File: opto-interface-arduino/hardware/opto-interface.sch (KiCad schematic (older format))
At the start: 24 parts, among them P1 CONN_02X06, P2 CONN_01X06, U1 LM7805, U2 LM7905

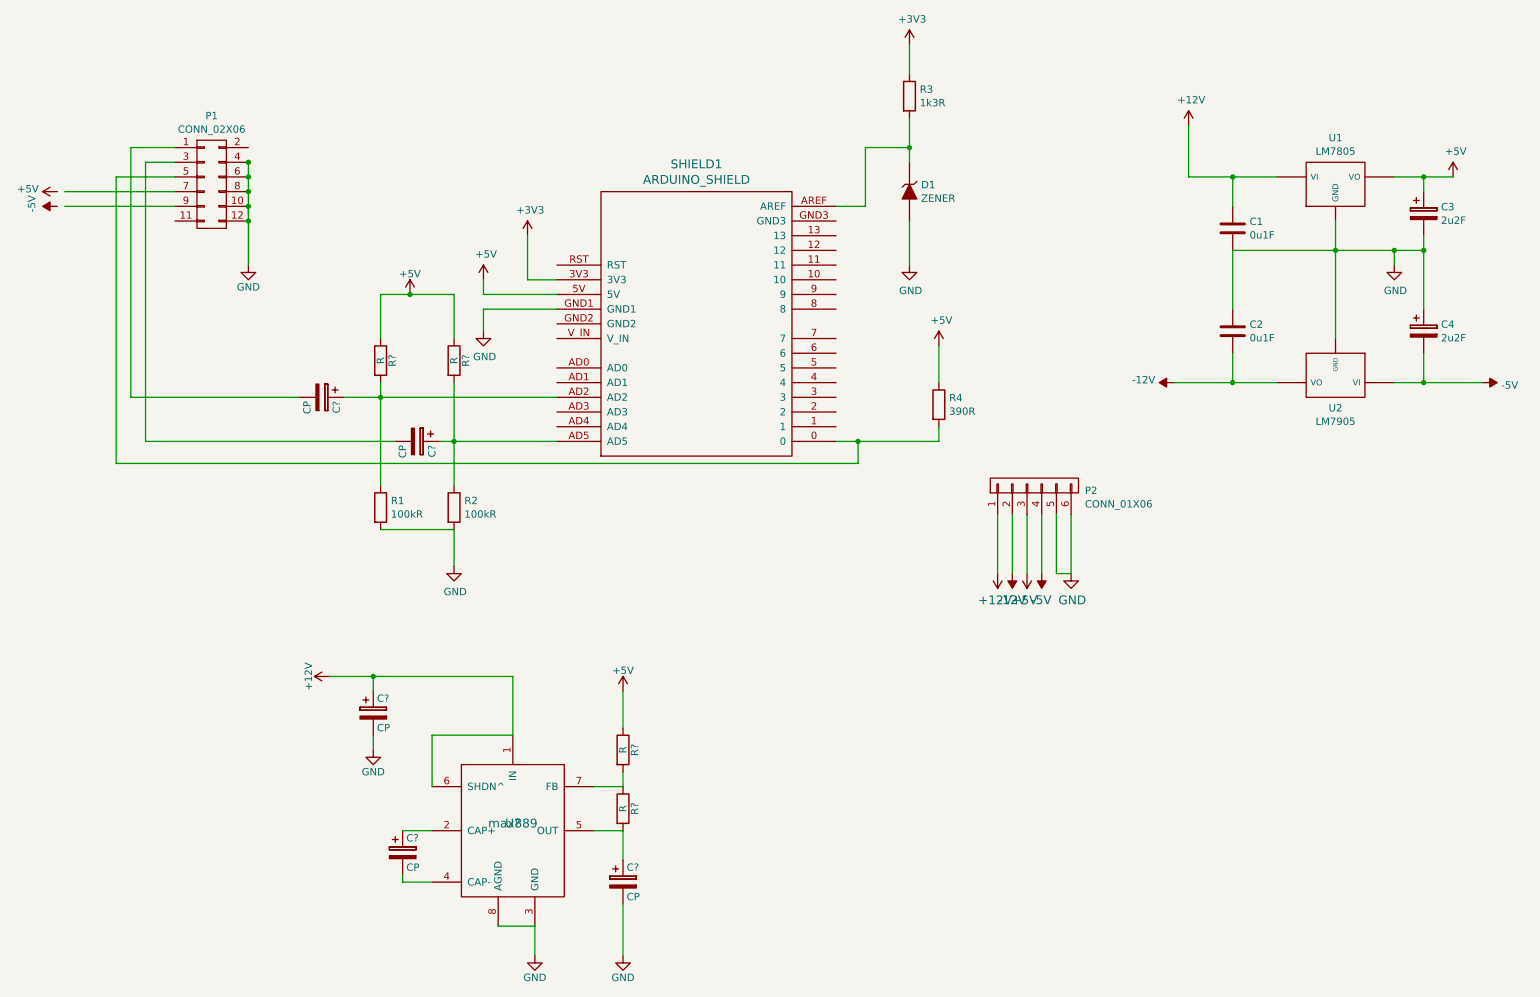
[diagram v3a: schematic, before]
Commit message: Add filter simulations, first pass layout, some calculations and some skeleton code.
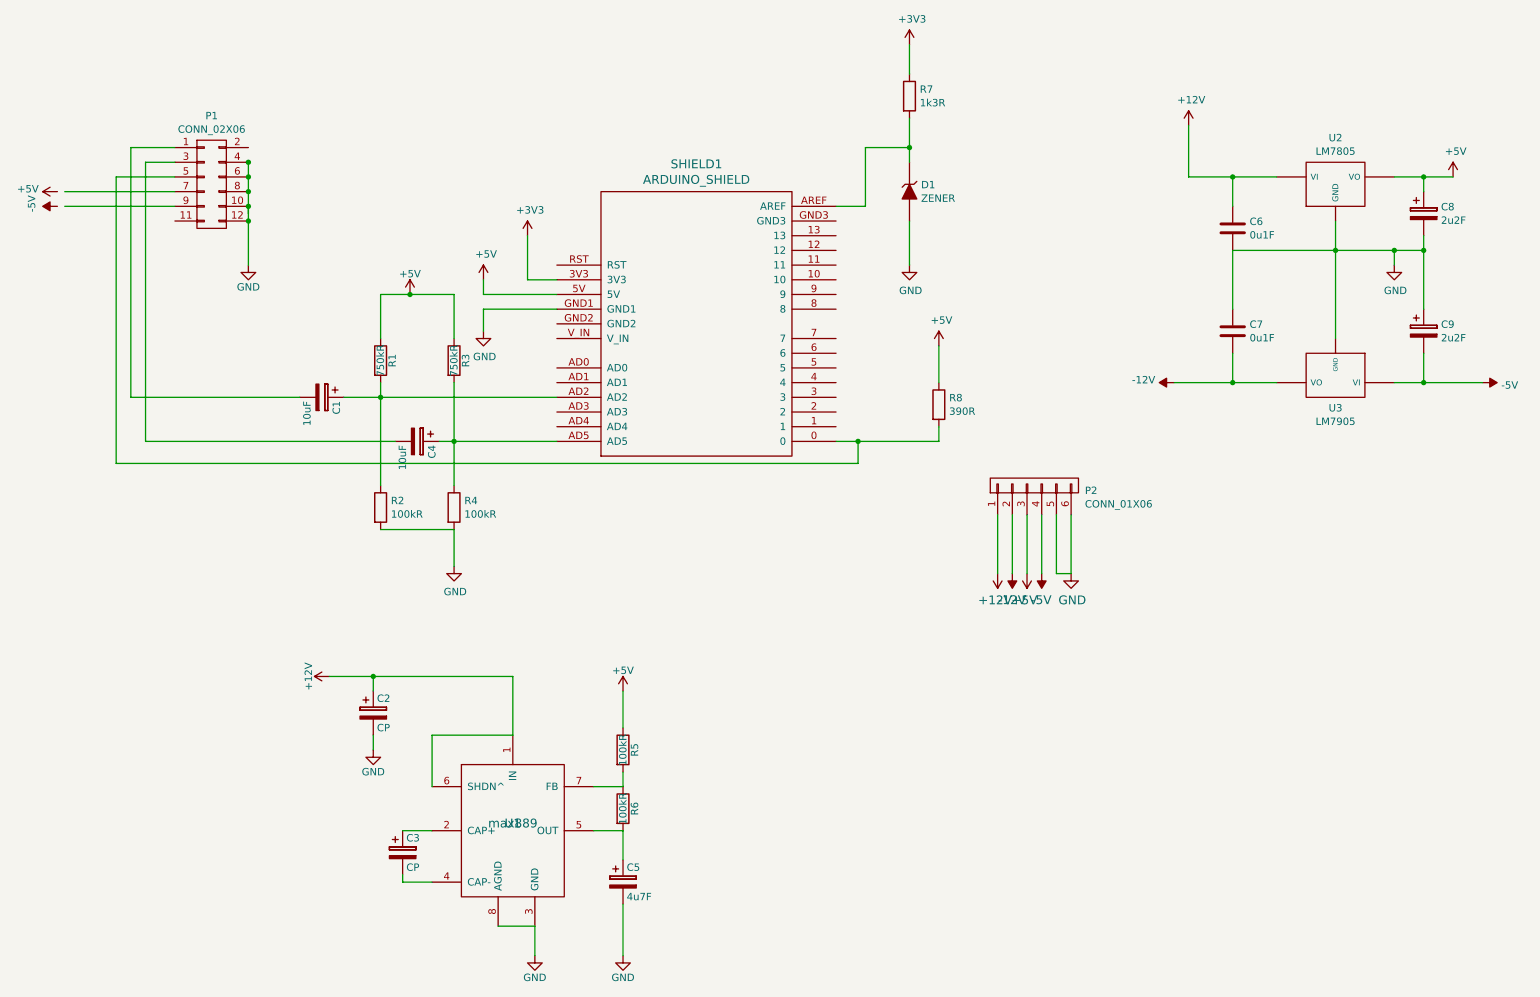
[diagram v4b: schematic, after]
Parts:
- C1, C4: renamed from C?; value CP -> 10uF; footprint (none) -> Discret:CP4
- C2, C3: renamed from C?; footprint (none) -> Capacitors_SMD:c_elec_8x5.4
- C5: renamed from C?; value CP -> 4u7F; footprint (none) -> Capacitors_SMD:c_elec_8x5.4
- R1, R3: renamed from R?; value R -> 750kR; footprint (none) -> Resistors_SMD:R_0805_HandSoldering
- R5, R6: renamed from R?; value R -> 100kR; footprint (none) -> Resistors_SMD:R_0805_HandSoldering
- U1: renamed from U?; footprint (none) -> SMD_Packages:SOIC-8-N
- U2: renamed from U1; footprint TO_SOT_Packages_THT:TO-220_Neutral123_Horizontal_LargePads -> regul:TO-220_regul_Horizontal_LargePads
- U3: renamed from U2; footprint TO_SOT_Packages_THT:TO-220_Neutral123_Horizontal_LargePads -> regul:TO-220_regul_Horizontal_LargePads
- renumbered C1 to C6, C2 to C7, C3 to C8, C4 to C9, R1 to R2, R2 to R4, R3 to R7, R4 to R8
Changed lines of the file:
@@
 $EndComp
 $Comp
-L R-RESCUE-opto-interface R4
+L R-RESCUE-opto-interface R8
 U 1 1 56A61D1F
 P 6600 3150
-F 0 "R4" H 6670 3196 50  0000 L CNN
+F 0 "R8" H 6670 3196 50  0000 L CNN
 F 1 "390R" H 6670 3104 50  0000 L CNN
 F 2 "Resistors_SMD:R_0805_HandSoldering" V 6530 3150 50  0001 C CNN
@@
 $EndComp
 $Comp
-L R-RESCUE-opto-interface R2
+L R-RESCUE-opto-interface R4
 U 1 1 56A61E09
 P 3300 3850
-F 0 "R2" H 3370 3896 50  0000 L CNN
+F 0 "R4" H 3370 3896 50  0000 L CNN
 F 1 "100kR" H 3370 3804 50  0000 L CNN
 F 2 "Resistors_SMD:R_0805_HandSoldering" V 3230 3850 50  0001 C CNN
@@
 $EndComp
 $Comp
-L R-RESCUE-opto-interface R1
+L R-RESCUE-opto-interface R2
 U 1 1 56A61E93
 P 2800 3850
-F 0 "R1" H 2870 3896 50  0000 L CNN
+F 0 "R2" H 2870 3896 50  0000 L CNN
 F 1 "100kR" H 2870 3804 50  0000 L CNN
 F 2 "Resistors_SMD:R_0805_HandSoldering" V 2730 3850 50  0001 C CNN
@@
 $EndComp
 $Comp
-L LM7805 U1
+L LM7805 U2
 U 1 1 56A63641
 P 9300 1650
-F 0 "U1" H 9300 1966 50  0000 C CNN
+F 0 "U2" H 9300 1966 50  0000 C CNN
 F 1 "LM7805" H 9300 1874 50  0000 C CNN
-F 2 "TO_SOT_Packages_THT:TO-220_Neutral123_Horizontal_LargePads" H 9300 1650 50  0001 C CNN
+F 2 "regul:TO-220_regul_Horizontal_LargePads" H 9300 1650 50  0001 C CNN
 F 3 "" H 9300 1650 50  0000 C CNN
 	1    9300 1650
@@
 	9700 1600 10100 1600
 $Comp
-L C-RESCUE-opto-interface C1
+L C-RESCUE-opto-interface C6
 U 1 1 56A63A9E
 P 8600 1950
-F 0 "C1" H 8715 1996 50  0000 L CNN
+F 0 "C6" H 8715 1996 50  0000 L CNN
 F 1 "0u1F" H 8715 1904 50  0000 L CNN
 F 2 "Capacitors_ThroughHole:C_Disc_D6_P5" H 8638 1800 50  0001 C CNN
@@
 Connection ~ 9300 2100
 $Comp
-L CP-RESCUE-opto-interface C3
+L CP-RESCUE-opto-interface C8
 U 1 1 56A63B52
 P 9900 1850
-F 0 "C3" H 10018 1896 50  0000 L CNN
+F 0 "C8" H 10018 1896 50  0000 L CNN
 F 1 "2u2F" H 10018 1804 50  0000 L CNN
 F 2 "Discret:CP5" H 9938 1700 50  0001 C CNN
@@
 Connection ~ 9700 2100
 $Comp
-L LM7905 U2
+L LM7905 U3
 U 1 1 56A63CED
 P 9300 2950
-F 0 "U2" H 9300 3173 50  0000 C CNN
+F 0 "U3" H 9300 3173 50  0000 C CNN
 F 1 "LM7905" H 9300 3265 50  0000 C CNN
-F 2 "TO_SOT_Packages_THT:TO-220_Neutral123_Horizontal_LargePads" H 9300 2950 50  0001 C CNN
+F 2 "regul:TO-220_regul_Horizontal_LargePads" H 9300 2950 50  0001 C CNN
 F 3 "" H 9300 2950 50  0000 C CNN
 	1    9300 2950
@@
 $EndComp
 $Comp
-L C-RESCUE-opto-interface C2
+L C-RESCUE-opto-interface C7
 U 1 1 56A63DBB
 P 8600 2650
-F 0 "C2" H 8715 2696 50  0000 L CNN
+F 0 "C7" H 8715 2696 50  0000 L CNN
 F 1 "0u1F" H 8715 2604 50  0000 L CNN
 F 2 "Capacitors_ThroughHole:C_Disc_D6_P5" H 8638 2500 50  0001 C CNN
@@
 $EndComp
 $Comp
-L CP-RESCUE-opto-interface C4
+L CP-RESCUE-opto-interface C9
 U 1 1 56A63E65
 P 9900 2650
-F 0 "C4" H 10018 2696 50  0000 L CNN
+F 0 "C9" H 10018 2696 50  0000 L CNN
 F 1 "2u2F" H 10018 2604 50  0000 L CNN
 F 2 "Discret:CP5" H 9938 2500 50  0001 C CNN
@@
 $EndComp
 $Comp
-L -12V #PWR15
+L -12V #PWR22
 U 1 1 56A63F07
 P 8200 3000
-F 0 "#PWR15" H 8200 3100 50  0001 C CNN
+F 0 "#PWR22" H 8200 3100 50  0001 C CNN
 F 1 "-12V" V 8218 3127 50  0000 L CNN
 F 2 "" H 8200 3000 50  0000 C CNN
@@
 Connection ~ 9900 2100
 $Comp
-L -5V #PWR19
+L -5V #PWR26
 U 1 1 56A640D9
 P 10300 3000
-F 0 "#PWR19" H 10300 3100 50  0001 C CNN
+F 0 "#PWR26" H 10300 3100 50  0001 C CNN
 F 1 "-5V" V 10318 3128 50  0000 L CNN
 F 2 "" H 10300 3000 50  0000 C CNN
@@
 Connection ~ 6400 1400
 $Comp
-L R-RESCUE-opto-interface R3
+L R-RESCUE-opto-interface R7
 U 1 1 56A8A23F
 P 6400 1050
-F 0 "R3" H 6470 1096 50  0000 L CNN
+F 0 "R7" H 6470 1096 50  0000 L CNN
 F 1 "1k3R" H 6470 1004 50  0000 L CNN
 F 2 "Resistors_SMD:R_0805_HandSoldering" V 6330 1050 50  0001 C CNN
@@
 $EndComp
 $Comp
-L -12V #PWR11
+L -12V #PWR18
 U 1 1 56B5E808
 P 7100 4300
-F 0 "#PWR11" H 7100 4400 20  0001 C CNN
+F 0 "#PWR18" H 7100 4400 20  0001 C CNN
 F 1 "-12V" H 7102 4480 60  0000 C CNN
 F 2 "" H 7100 4300 60  0000 C CNN
@@
 $EndComp
 $Comp
-L -5V #PWR13
+L -5V #PWR20
 U 1 1 56B5E862
 P 7300 4300
-F 0 "#PWR13" H 7300 4400 20  0001 C CNN
+F 0 "#PWR20" H 7300 4400 20  0001 C CNN
 F 1 "-5V" H 7302 4480 60  0000 C CNN
 F 2 "" H 7300 4300 60  0000 C CNN
@@
 	7500 4300 7500 3900
 $Comp
-L max889 U?
+L max889 U1
 U 1 1 56D83630
 P 3700 6000
-F 0 "U?" H 3700 6000 60  0000 C CNN
+F 0 "U1" H 3700 6000 60  0000 C CNN
 F 1 "max889" H 3700 6000 60  0000 C CNN
-F 2 "" H 3700 6000 60  0000 C CNN
+F 2 "SMD_Packages:SOIC-8-N" H 3700 6000 60  0001 C CNN
 F 3 "" H 3700 6000 60  0000 C CNN
 	1    3700 6000
@@
 $EndComp
 $Comp
-L +12V #PWR?
+L +12V #PWR015
 U 1 1 56D96E3B
 P 2450 5000
-F 0 "#PWR?" H 2450 4850 50  0001 C CNN
+F 0 "#PWR015" H 2450 4850 50  0001 C CNN
 F 1 "+12V" H 2450 5140 50  0000 C CNN
 F 2 "" H 2450 5000 50  0000 C CNN
@@
 $EndComp
 $Comp
-L CP C?
+L CP C2
 U 1 1 56D96E9A
 P 2750 5250
-F 0 "C?" H 2775 5350 50  0000 L CNN
+F 0 "C2" H 2775 5350 50  0000 L CNN
 F 1 "CP" H 2775 5150 50  0000 L CNN
-F 2 "" H 2788 5100 50  0000 C CNN
+F 2 "Capacitors_SMD:c_elec_8x5.4" H 2788 5100 50  0001 C CNN
 F 3 "" H 2750 5250 50  0000 C CNN
 	1    2750 5250
@@
 $EndComp
 $Comp
-L GND #PWR?
+L GND #PWR016
 U 1 1 56D96EFB
 P 2750 5500
-F 0 "#PWR?" H 2750 5250 50  0001 C CNN
+F 0 "#PWR016" H 2750 5250 50  0001 C CNN
 F 1 "GND" H 2750 5350 50  0000 C CNN
 F 2 "" H 2750 5500 50  0000 C CNN
@@
 	2750 5400 2750 5500
 $Comp
-L R R?
+L R R6
 U 1 1 56D97041
 P 4450 5900
-F 0 "R?" V 4530 5900 50  0000 C CNN
-F 1 "R" V 4450 5900 50  0000 C CNN
-F 2 "" V 4380 5900 50  0000 C CNN
+F 0 "R6" V 4530 5900 50  0000 C CNN
+F 1 "100kR" V 4450 5900 50  0000 C CNN
+F 2 "Resistors_SMD:R_0805_HandSoldering" V 4380 5900 50  0001 C CNN
 F 3 "" H 4450 5900 50  0000 C CNN
 	1    4450 5900
@@
 $EndComp
 $Comp
-L GND #PWR?
+L GND #PWR017
 U 1 1 56D97092
 P 3850 6900
-F 0 "#PWR?" H 3850 6650 50  0001 C CNN
+F 0 "#PWR017" H 3850 6650 50  0001 C CNN
 F 1 "GND" H 3850 6750 50  0000 C CNN
 F 2 "" H 3850 6900 50  0000 C CNN
@@
 	3850 6700 3850 6900
 $Comp
-L CP C?
+L CP C3
 U 1 1 56D971F2
 P 2950 6200
-F 0 "C?" H 2975 6300 50  0000 L CNN
+F 0 "C3" H 2975 6300 50  0000 L CNN
 F 1 "CP" H 2975 6100 50  0000 L CNN
-F 2 "" H 2988 6050 50  0000 C CNN
+F 2 "Capacitors_SMD:c_elec_8x5.4" H 2988 6050 50  0001 C CNN
 F 3 "" H 2950 6200 50  0000 C CNN
 	1    2950 6200
@@
 	3150 5400 3700 5400
 $Comp
-L R R?
+L R R5
 U 1 1 56D97445
 P 4450 5500
-F 0 "R?" V 4530 5500 50  0000 C CNN
-F 1 "R" V 4450 5500 50  0000 C CNN
-F 2 "" V 4380 5500 50  0000 C CNN
+F 0 "R5" V 4530 5500 50  0000 C CNN
+F 1 "100kR" V 4450 5500 50  0000 C CNN
+F 2 "Resistors_SMD:R_0805_HandSoldering" V 4380 5500 50  0001 C CNN
 F 3 "" H 4450 5500 50  0000 C CNN
 	1    4450 5500
@@
 $EndComp
 $Comp
-L CP C?
+L CP C5
 U 1 1 56D974A2
 P 4450 6400
-F 0 "C?" H 4475 6500 50  0000 L CNN
-F 1 "CP" H 4475 6300 50  0000 L CNN
-F 2 "" H 4488 6250 50  0000 C CNN
+F 0 "C5" H 4475 6500 50  0000 L CNN
+F 1 "4u7F" H 4475 6300 50  0000 L CNN
+F 2 "Capacitors_SMD:c_elec_8x5.4" H 4488 6250 50  0001 C CNN
 F 3 "" H 4450 6400 50  0000 C CNN
 	1    4450 6400
@@
 	4450 5750 4450 5650
 $Comp
-L GND #PWR?
+L GND #PWR018
 U 1 1 56D975F0
 P 4450 6900
-F 0 "#PWR?" H 4450 6650 50  0001 C CNN
+F 0 "#PWR018" H 4450 6650 50  0001 C CNN
 F 1 "GND" H 4450 6750 50  0000 C CNN
 F 2 "" H 4450 6900 50  0000 C CNN
@@
 	4450 6550 4450 6900
 $Comp
-L +5V #PWR?
+L +5V #PWR019
 U 1 1 56D9A3A4
 P 4450 5100
-F 0 "#PWR?" H 4450 4950 50  0001 C CNN
+F 0 "#PWR019" H 4450 4950 50  0001 C CNN
 F 1 "+5V" H 4450 5240 50  0000 C CNN
 F 2 "" H 4450 5100 50  0000 C CNN
@@
 	4450 5100 4450 5350
 $Comp
-L GND #PWR?
+L GND #PWR020
 U 1 1 56D9BC76
 P 1900 2200
-F 0 "#PWR?" H 1900 1950 50  0001 C CNN
+F 0 "#PWR020" H 1900 1950 50  0001 C CNN
 F 1 "GND" H 1900 2050 50  0000 C CNN
 F 2 "" H 1900 2200 50  0000 C CNN
@@
 	1900 1800 1900 2200
 $Comp
-L R R?
+L R R1
 U 1 1 56D9C093
 P 2800 2850
-F 0 "R?" V 2880 2850 50  0000 C CNN
-F 1 "R" V 2800 2850 50  0000 C CNN
-F 2 "" V 2730 2850 50  0000 C CNN
+F 0 "R1" V 2880 2850 50  0000 C CNN
+F 1 "750kR" V 2800 2850 50  0000 C CNN
+F 2 "Resistors_SMD:R_0805_HandSoldering" V 2730 2850 50  0001 C CNN
 F 3 "" H 2800 2850 50  0000 C CNN
 	1    2800 2850
@@
 $EndComp
 $Comp
-L R R?
+L R R3
 U 1 1 56D9C122
 P 3300 2850
-F 0 "R?" V 3380 2850 50  0000 C CNN
-F 1 "R" V 3300 2850 50  0000 C CNN
-F 2 "" V 3230 2850 50  0000 C CNN
+F 0 "R3" V 3380 2850 50  0000 C CNN
+F 1 "750kR" V 3300 2850 50  0000 C CNN
+F 2 "Resistors_SMD:R_0805_HandSoldering" V 3230 2850 50  0001 C CNN
 F 3 "" H 3300 2850 50  0000 C CNN
 	1    3300 2850
@@
 $EndComp
 $Comp
-L +5V #PWR?
+L +5V #PWR021
 U 1 1 56D9C2D5
 P 3000 2400
-F 0 "#PWR?" H 3000 2250 50  0001 C CNN
+F 0 "#PWR021" H 3000 2250 50  0001 C CNN
 F 1 "+5V" H 3000 2540 50  0000 C CNN
 F 2 "" H 3000 2400 50  0000 C CNN
@@
 Connection ~ 3000 2400
 $Comp
-L CP C?
+L CP C1
 U 1 1 56D9C415
 P 2400 3100
-F 0 "C?" H 2425 3200 50  0000 L CNN
-F 1 "CP" H 2425 3000 50  0000 L CNN
-F 2 "" H 2438 2950 50  0000 C CNN
+F 0 "C1" H 2425 3200 50  0000 L CNN
+F 1 "10uF" H 2425 3000 50  0000 L CNN
+F 2 "Discret:CP4" H 2438 2950 50  0001 C CNN
 F 3 "" H 2400 3100 50  0000 C CNN
 	1    2400 3100
@@
 $EndComp
 $Comp
-L CP C?
+L CP C4
 U 1 1 56D9C4C2
 P 3050 3400
-F 0 "C?" H 3075 3500 50  0000 L CNN
-F 1 "CP" H 3075 3300 50  0000 L CNN
-F 2 "" H 3088 3250 50  0000 C CNN
+F 0 "C4" H 3075 3500 50  0000 L CNN
+F 1 "10uF" H 3075 3300 50  0000 L CNN
+F 2 "Discret:CP4" H 3088 3250 50  0001 C CNN
 F 3 "" H 3050 3400 50  0000 C CNN
 	1    3050 3400
